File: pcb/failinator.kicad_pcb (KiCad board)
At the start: 2 copper layers, 65 x 56 mm, 22 parts, among them P1 CONN_01X04, P2 CONN_01X10, P3 CONN_01X10, P4 CONN_01X06, U1 MAX7219, U2 RASPIPLUSHEADER

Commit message: Starting work on revision v0.2.
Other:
- board text added: "v0.2"
- board text removed: "v0.1"
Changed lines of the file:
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@@
   )
   (page A4)
+  (title_block
+    (rev v0.2)
+  )
   (layers
     (0 F.Cu mixed)
@@
     )
   )
-  (gr_text v0.1 (at 107.5 120) (layer F.SilkS)
+  (gr_text v0.2 (at 107.5 120) (layer F.SilkS)
     (effects (font (size 1.5 1.5) (thickness 0.3)))
   )

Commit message: Factor out the MOSFET switches into a separate sheet.
There will be a lot more of these soon once we start using a similar
pattern to switch the LED segments.
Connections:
- net /AMBER_L renamed /AmberDriver/EN
- net /AMBER_P renamed /AmberDriver/VOUT
- net /GREEN_L renamed /GreenDriver/EN
- net /GREEN_P renamed /GreenDriver/VOUT
- net /RED_L renamed /RedDriver/EN
- net /RED_P renamed /RedDriver/VOUT

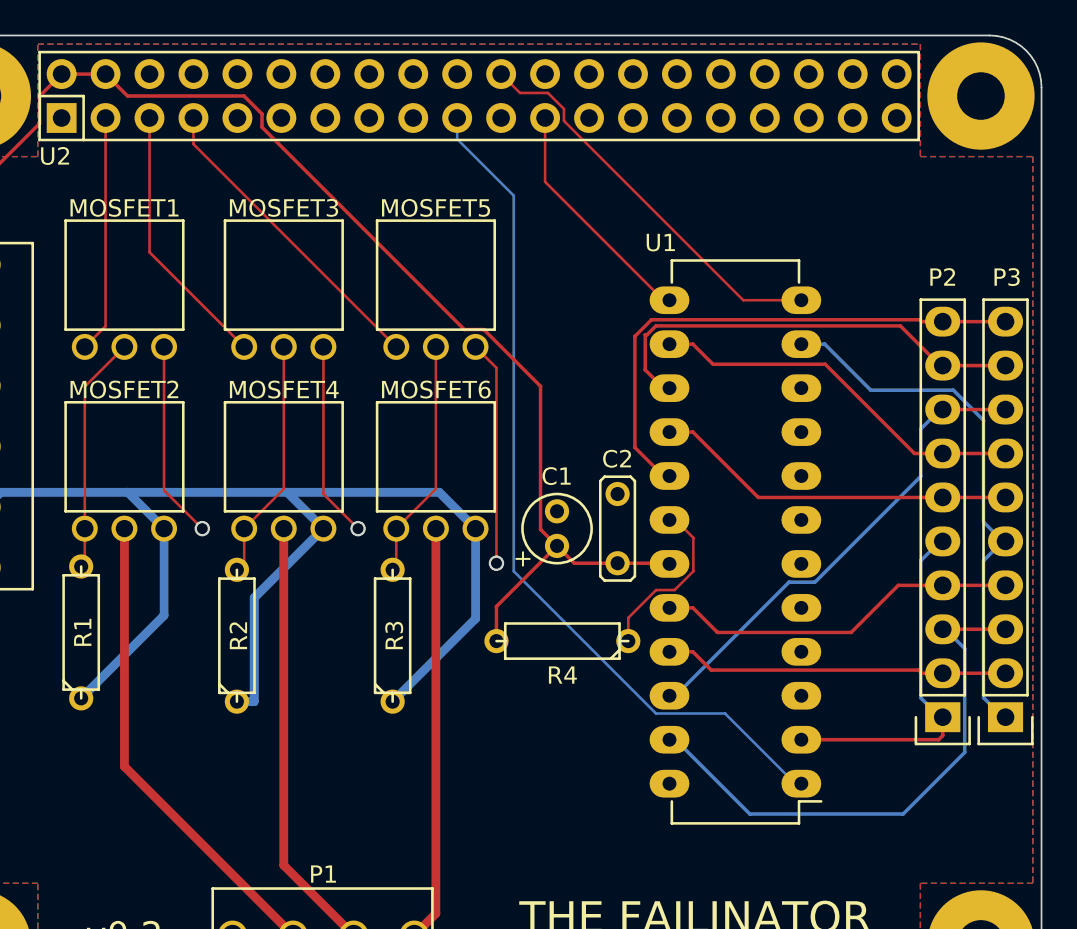
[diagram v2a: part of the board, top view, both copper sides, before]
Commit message: Remove the MAX7219-based digit driver sub-circuit
The digit driver on v0.1 was not correct, providing only 5V to LED
segments that have a forward voltage of more like 27V, causing them to
not show at all.

A replacement for this will be added in a subsequent commit.
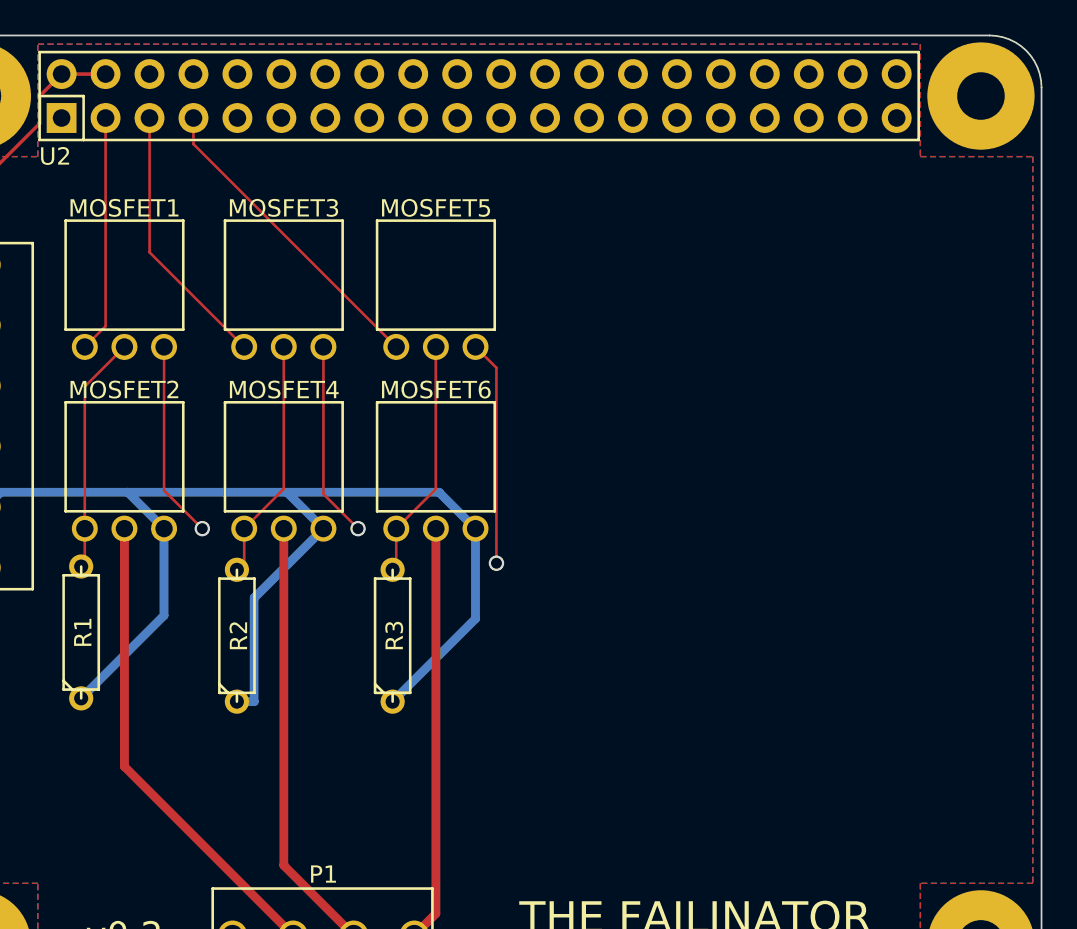
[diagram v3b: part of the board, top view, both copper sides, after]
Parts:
- removed C1: 10u, failinator:CPOL_2mm
- removed C2: 100n, failinator:C_4mm
- removed P2, P3: CONN_01X10, Pin_Headers:Pin_Header_Straight_1x10
- removed R4: R, Discret:R3
- removed U1: MAX7219, Housings_DIP:DIP-24_W7.62mm_LongPads
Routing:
- net +5V: track 77.1 -> 20.5 mm
- net /MOSI: track 49.4 -> 0.14 mm
- net /SEGD: track 31.8 -> 0.00 mm
- net /DIG1: track 31.6 -> 0.00 mm
- net /SEGG: track 31.0 -> 0.00 mm
- net /SEGDP: track 28.0 -> 0.00 mm
- net /SEGF: track 26.0 -> 0.00 mm
- net /DISP_CS: track 23.4 -> 0.24 mm
- net /SEGA: track 22.5 -> 0.00 mm
- net /SEGB: track 21.3 -> 0.00 mm
- net /SEGC: track 21.1 -> 0.00 mm
- net /DIG0: track 21.1 -> 0.00 mm
- net /SEGE: track 20.1 -> 0.00 mm
- net /SCLK: track 13.7 -> 0.00 mm
- net Net-(R4-Pad1): track 9.96 -> 0.00 mm

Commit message: Start of 7seg display board floor planning
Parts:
- added C1: C_Small, Capacitors_SMD:C_0805_HandSoldering, F.Cu at (135.0, 134.0)
- added C2: C_Small, Capacitors_SMD:C_0805_HandSoldering, F.Cu at (153.0, 131.5)
- added MOSFET10: FQU17P06, failinator:TO-251AA, F.Cu at (90.5, 157.5)
- added MOSFET11: FQU13N06L, failinator:TO-251AA, F.Cu at (75.0, 171.5)
- added MOSFET12: FQU17P06, failinator:TO-251AA, F.Cu at (56.5, 170.0)
- added MOSFET13: FQU13N06L, failinator:TO-251AA, F.Cu at (56.5, 149.5)
- added MOSFET14: FQU17P06, failinator:TO-251AA, F.Cu at (59.8, 129.5)
- added MOSFET15: FQU13N06L, failinator:TO-251AA, F.Cu at (274.0, 58.0)
- added MOSFET16: FQU17P06, failinator:TO-251AA, F.Cu at (284.5, 58.0)
- added MOSFET17: FQU13N06L, failinator:TO-251AA, F.Cu at (39.0, 158.0)
- added MOSFET18: FQU17P06, failinator:TO-251AA, F.Cu at (37.5, 179.5)
- added MOSFET19: FQU13N06L, failinator:TO-251AA, F.Cu at (57.5, 185.5)
- added MOSFET20: FQU17P06, failinator:TO-251AA, F.Cu at (83.2, 184.5)
- added MOSFET21: FQU13N06L, failinator:TO-251AA, F.Cu at (103.0, 182.0)
- added MOSFET22: FQU17P06, failinator:TO-251AA, F.Cu at (120.0, 174.5)
- added MOSFET23: FQU13N06L, failinator:TO-251AA, F.Cu at (131.5, 174.5)
- added MOSFET24: FQU17P06, failinator:TO-251AA, F.Cu at (147.5, 175.0)
- added MOSFET25: FQU13N06L, failinator:TO-251AA, F.Cu at (137.5, 158.0)
- added MOSFET26: FQU17P06, failinator:TO-251AA, F.Cu at (103.0, 165.5)
- added MOSFET27: FQU13N06L, failinator:TO-251AA, F.Cu at (115.0, 188.0)
- added MOSFET28: FQU17P06, failinator:TO-251AA, F.Cu at (126.7, 188.5)
- added MOSFET29: FQU13N06L, failinator:TO-251AA, F.Cu at (140.2, 188.0)
- added MOSFET30: FQU17P06, failinator:TO-251AA, F.Cu at (98.5, 192.0)
- added MOSFET31: FQU13N06L, failinator:TO-251AA, F.Cu at (70.5, 196.5)
- added MOSFET32: FQU17P06, failinator:TO-251AA, F.Cu at (46.8, 192.5)
- added MOSFET33: FQU13N06L, failinator:TO-251AA, F.Cu at (32.5, 193.5)
- added MOSFET34: FQU17P06, failinator:TO-251AA, F.Cu at (21.5, 164.5)
- added MOSFET7: FQU13N06L, failinator:TO-251AA, F.Cu at (78.2, 141.5)
- added MOSFET8: FQU17P06, failinator:TO-251AA, F.Cu at (91.0, 138.5)
- added MOSFET9: FQU13N06L, failinator:TO-251AA, F.Cu at (71.7, 156.0)
- added P2: CONN_01X06, failinator:Wire_Conn_6pin_StrainReliefRight, F.Cu at (155.5, 89.4)
- added P3: CONN_01X06, Pin_Headers:Pin_Header_Straight_1x06, F.Cu at (240.5, 64.5)
- added R10: 10k, Discret:R3, F.Cu at (128.7, 144.5)
- added R11: 10k, Discret:R3, F.Cu at (117.2, 142.0)
- added R12: 10k, Discret:R3, F.Cu at (115.2, 137.0)
- added R13: 10k, Discret:R3, F.Cu at (114.7, 132.0)
- added R14: 10k, Discret:R3, F.Cu at (118.7, 128.0)
- added R15: 10k, Discret:R3, F.Cu at (130.2, 128.5)
- added R16: 10k, Discret:R3, F.Cu at (131.7, 140.5)
- added R17: 10k, Discret:R3, F.Cu at (118.2, 145.5)
- added R18: 10k, Resistors_SMD:R_0805_HandSoldering, F.Cu at (156.0, 140.5)
- added R19: 10k, Resistors_SMD:R_0805_HandSoldering, F.Cu at (156.0, 147.0)
- added R4: 10k, Discret:R3, F.Cu at (145.7, 136.5)
- added R5: 10k, Discret:R3, F.Cu at (144.7, 133.0)
- added R6: 10k, Discret:R3, F.Cu at (143.7, 139.5)
- added R7: 10k, Discret:R3, F.Cu at (143.2, 142.5)
- added R8: 10k, Discret:R3, F.Cu at (142.2, 129.5)
- added R9: 10k, Discret:R3, F.Cu at (141.7, 145.5)
- added U1: 74HC594, Housings_SOIC:SOIC-16_3.9x9.9mm_Pitch1.27mm, F.Cu at (247.5, 55.5)
- added U3: LDS-CD16RI, failinator:LDS-CD16RI, B.Cu at (271.8, 34.9)
- added U4: LDS-CD16RI, failinator:LDS-CD16RI, B.Cu at (223.9, 34.9)
- added U5: 74HC594, Housings_SOIC:SOIC-16_3.9x9.9mm_Pitch1.27mm, F.Cu at (247.5, 44.0)
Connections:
- U2 pad 22: /DISP_CS -> Net-(U2-Pad22)
- U2 pad 24: Net-(U2-Pad24) -> /DISP_CS
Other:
- board size 65 x 56 mm -> 200 x 124 mm

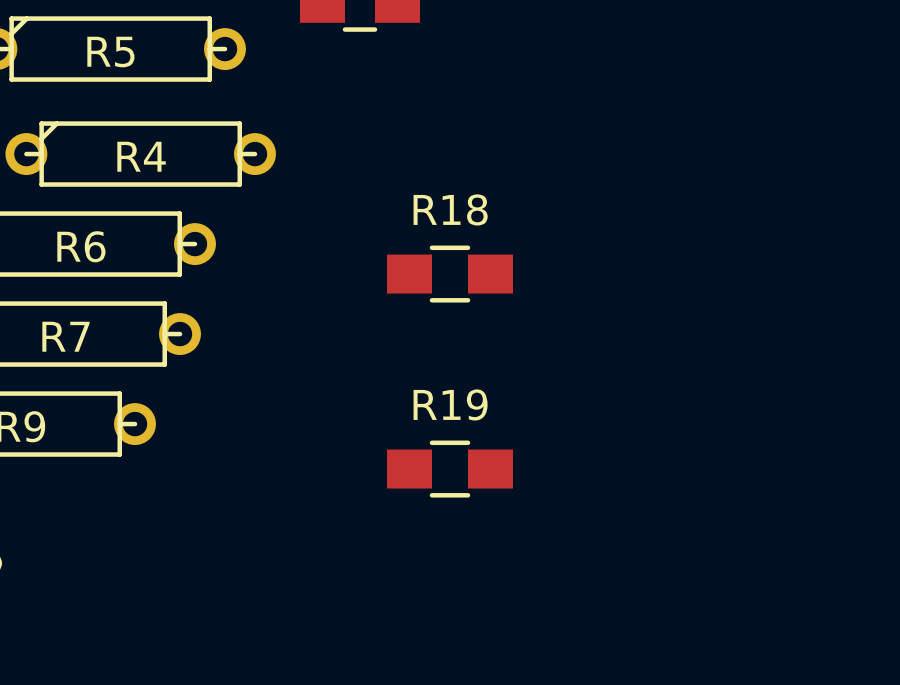
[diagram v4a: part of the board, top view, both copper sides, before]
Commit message: Use through-hole footprints for all display board resistors
Previously two of them were incorrectly set to 0805 SMD footprints.

I actually expect the display board layout is going to be very cramped
so these might actually all become 0805s later, but going to try with
through-hole first because I don't relish the thought of hand-soldering
14 0805 resistors in a single sitting.
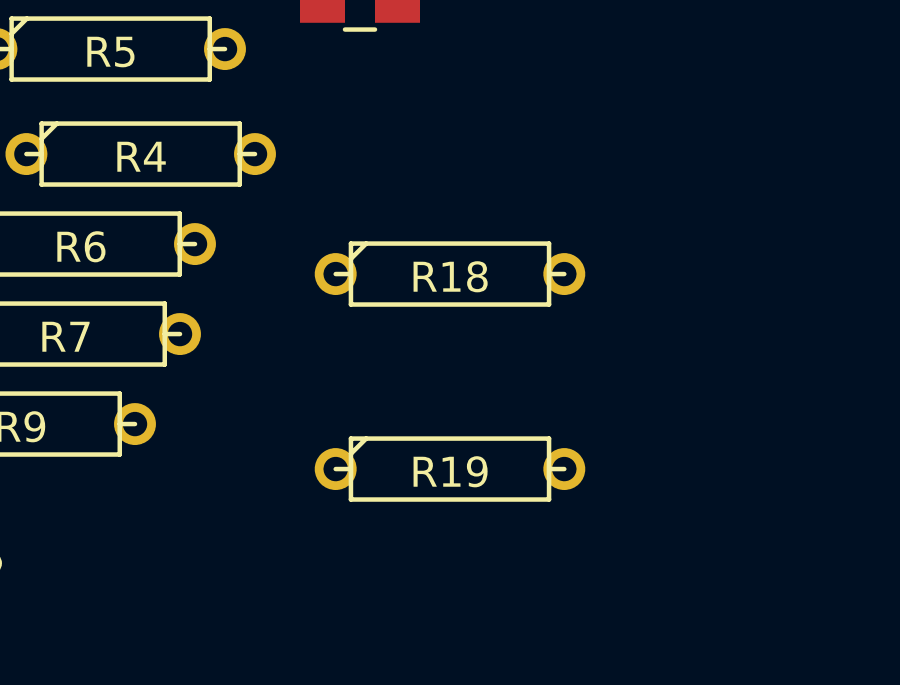
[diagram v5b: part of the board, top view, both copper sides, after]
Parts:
- R18, R19: footprint Resistors_SMD:R_0805_HandSoldering -> Discret:R3
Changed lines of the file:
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@@
   (general
     (links 164)
-    (no_connects 79)
-    (area 95.449999 67.949999 160.550001 124.050001)
+    (no_connects 127)
+    (area 95.449999 -0.050001 295.550001 124.050001)
     (thickness 1.6)
     (drawings 16)
@@
     )
   )
-  (module Resistors_SMD:R_0805_HandSoldering (layer F.Cu)
-    (at 156 140.5)
-    (descr "Resistor SMD 0805, hand soldering")
-    (tags "resistor 0805")
-    (attr smd)
-    (fp_text reference R18 (at 0 -2.1) (layer F.SilkS)
-      (effects (font (size 1 1) (thickness 0.15)))
-    )
-    (fp_text value 10k (at 0 2.1) (layer F.Fab)
-      (effects (font (size 1 1) (thickness 0.15)))
-    )
-    (fp_line (start -2.4 -1) (end 2.4 -1) (layer F.CrtYd) (width 0.05))
-    (fp_line (start -2.4 1) (end 2.4 1) (layer F.CrtYd) (width 0.05))
-    (fp_line (start -2.4 -1) (end -2.4 1) (layer F.CrtYd) (width 0.05))
-    (fp_line (start 2.4 -1) (end 2.4 1) (layer F.CrtYd) (width 0.05))
-    (fp_line (start 0.6 0.875) (end -0.6 0.875) (layer F.SilkS) (width 0.15))
-    (fp_line (start -0.6 -0.875) (end 0.6 -0.875) (layer F.SilkS) (width 0.15))
-    (pad 1 smd rect (at -1.35 0) (size 1.5 1.3) (layers F.Cu F.Paste F.Mask)
-      (net 86 "Net-(R18-Pad1)"))
-    (pad 2 smd rect (at 1.35 0) (size 1.5 1.3) (layers F.Cu F.Paste F.Mask)
-      (net 39 /D_+3V3))
-    (model Resistors_SMD.3dshapes/R_0805_HandSoldering.wrl
-      (at (xyz 0 0 0))
-      (scale (xyz 1 1 1))
-      (rotate (xyz 0 0 0))
-    )
-  )
-  (module Resistors_SMD:R_0805_HandSoldering (layer F.Cu)
-    (at 156 147)
-    (descr "Resistor SMD 0805, hand soldering")
-    (tags "resistor 0805")
-    (attr smd)
-    (fp_text reference R19 (at 0 -2.1) (layer F.SilkS)
-      (effects (font (size 1 1) (thickness 0.15)))
-    )
-    (fp_text value 10k (at 0 2.1) (layer F.Fab)
-      (effects (font (size 1 1) (thickness 0.15)))
-    )
-    (fp_line (start -2.4 -1) (end 2.4 -1) (layer F.CrtYd) (width 0.05))
-    (fp_line (start -2.4 1) (end 2.4 1) (layer F.CrtYd) (width 0.05))
-    (fp_line (start -2.4 -1) (end -2.4 1) (layer F.CrtYd) (width 0.05))
-    (fp_line (start 2.4 -1) (end 2.4 1) (layer F.CrtYd) (width 0.05))
-    (fp_line (start 0.6 0.875) (end -0.6 0.875) (layer F.SilkS) (width 0.15))
-    (fp_line (start -0.6 -0.875) (end 0.6 -0.875) (layer F.SilkS) (width 0.15))
-    (pad 1 smd rect (at -1.35 0) (size 1.5 1.3) (layers F.Cu F.Paste F.Mask)
-      (net 87 "Net-(R19-Pad1)"))
-    (pad 2 smd rect (at 1.35 0) (size 1.5 1.3) (layers F.Cu F.Paste F.Mask)
-      (net 39 /D_+3V3))
-    (model Resistors_SMD.3dshapes/R_0805_HandSoldering.wrl
-      (at (xyz 0 0 0))
-      (scale (xyz 1 1 1))
-      (rotate (xyz 0 0 0))
-    )
-  )
   (module Housings_SOIC:SOIC-16_3.9x9.9mm_Pitch1.27mm (layer F.Cu)
     (at 247.5 55.5 270)
@@
       (rotate (xyz 0 0 0))
     )
+  )
+  (module Discret:R3 (layer F.Cu)
+    (at 156 140.5)
+    (descr "Resitance 3 pas")
+    (tags R)
+    (fp_text reference R18 (at 0 0.127) (layer F.SilkS)
+      (effects (font (size 1 1) (thickness 0.15)))
+    )
+    (fp_text value 10k (at 0 0.127) (layer F.Fab)
+      (effects (font (size 1 1) (thickness 0.15)))
+    )
+    (fp_line (start -3.81 0) (end -3.302 0) (layer F.SilkS) (width 0.15))
+    (fp_line (start 3.81 0) (end 3.302 0) (layer F.SilkS) (width 0.15))
+    (fp_line (start 3.302 0) (end 3.302 -1.016) (layer F.SilkS) (width 0.15))
+    (fp_line (start 3.302 -1.016) (end -3.302 -1.016) (layer F.SilkS) (width 0.15))
+    (fp_line (start -3.302 -1.016) (end -3.302 1.016) (layer F.SilkS) (width 0.15))
+    (fp_line (start -3.302 1.016) (end 3.302 1.016) (layer F.SilkS) (width 0.15))
+    (fp_line (start 3.302 1.016) (end 3.302 0) (layer F.SilkS) (width 0.15))
+    (fp_line (start -3.302 -0.508) (end -2.794 -1.016) (layer F.SilkS) (width 0.15))
+    (pad 1 thru_hole circle (at -3.81 0) (size 1.397 1.397) (drill 0.8128) (layers *.Cu *.Mask F.SilkS)
+      (net 86 "Net-(R18-Pad1)"))
+    (pad 2 thru_hole circle (at 3.81 0) (size 1.397 1.397) (drill 0.8128) (layers *.Cu *.Mask F.SilkS)
+      (net 39 /D_+3V3))
+    (model Discret.3dshapes/R3.wrl
+      (at (xyz 0 0 0))
+      (scale (xyz 0.3 0.3 0.3))
+      (rotate (xyz 0 0 0))
+    )
+  )
+  (module Discret:R3 (layer F.Cu)
+    (at 156 147)
+    (descr "Resitance 3 pas")
+    (tags R)
+    (fp_text reference R19 (at 0 0.127) (layer F.SilkS)
+      (effects (font (size 1 1) (thickness 0.15)))
+    )
+    (fp_text value 10k (at 0 0.127) (layer F.Fab)
+      (effects (font (size 1 1) (thickness 0.15)))
+    )
+    (fp_line (start -3.81 0) (end -3.302 0) (layer F.SilkS) (width 0.15))
+    (fp_line (start 3.81 0) (end 3.302 0) (layer F.SilkS) (width 0.15))
+    (fp_line (start 3.302 0) (end 3.302 -1.016) (layer F.SilkS) (width 0.15))
+    (fp_line (start 3.302 -1.016) (end -3.302 -1.016) (layer F.SilkS) (width 0.15))
+    (fp_line (start -3.302 -1.016) (end -3.302 1.016) (layer F.SilkS) (width 0.15))
+    (fp_line (start -3.302 1.016) (end 3.302 1.016) (layer F.SilkS) (width 0.15))
+    (fp_line (start 3.302 1.016) (end 3.302 0) (layer F.SilkS) (width 0.15))
+    (fp_line (start -3.302 -0.508) (end -2.794 -1.016) (layer F.SilkS) (width 0.15))
+    (pad 1 thru_hole circle (at -3.81 0) (size 1.397 1.397) (drill 0.8128) (layers *.Cu *.Mask F.SilkS)
+      (net 87 "Net-(R19-Pad1)"))
+    (pad 2 thru_hole circle (at 3.81 0) (size 1.397 1.397) (drill 0.8128) (layers *.Cu *.Mask F.SilkS)
+      (net 39 /D_+3V3))
+    (model Discret.3dshapes/R3.wrl
+      (at (xyz 0 0 0))
+      (scale (xyz 0.3 0.3 0.3))
+      (rotate (xyz 0 0 0))
+    )

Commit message: Placement of display 0 MOSFETs and resistors
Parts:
- moved MOSFET18 291.5 mm to (281.5, 20.0), turned to 90 degrees
- moved MOSFET19 275.2 mm to (271.5, 12.5), turned to 90 degrees
- moved MOSFET17 270.4 mm to (271.5, 20.0), turned to 90 degrees
- moved MOSFET20 262.5 mm to (281.5, 12.5), turned to 90 degrees
- moved MOSFET12 258.6 mm to (281.5, 42.5), turned to 90 degrees
- moved MOSFET13 236.9 mm to (271.5, 50.0), turned to 90 degrees
- moved MOSFET14 235.5 mm to (281.5, 50.0), turned to 90 degrees
- moved MOSFET11 235.1 mm to (271.5, 42.5), turned to 90 degrees
- moved MOSFET9 233.6 mm to (271.5, 35.0), turned to 90 degrees
- moved MOSFET10 226.9 mm to (281.5, 35.0), turned to 90 degrees
- moved MOSFET7 224.4 mm to (271.5, 27.5), turned to 90 degrees
- moved MOSFET8 220.5 mm to (281.5, 27.5), turned to 90 degrees
- moved R10 208.5 mm to (289.5, 11.8), turned to 90 degrees
- moved R9 191.8 mm to (286.5, 19.7), turned to 270 degrees
- moved R4 180.6 mm to (289.5, 27.2), turned to 270 degrees
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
